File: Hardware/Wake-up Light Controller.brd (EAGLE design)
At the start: 85.7 x 54 mm, 47 parts, among them IC1 ST1S10, IC2 HT7333, IC3 DS3231/SO, IC4 ATMEGA328P_TQFP, J1 AVR-ISP, J2 Debug, J3 CR1632_3V, Q1 BSS138, Q2 BSS138, Q3 FDN306P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

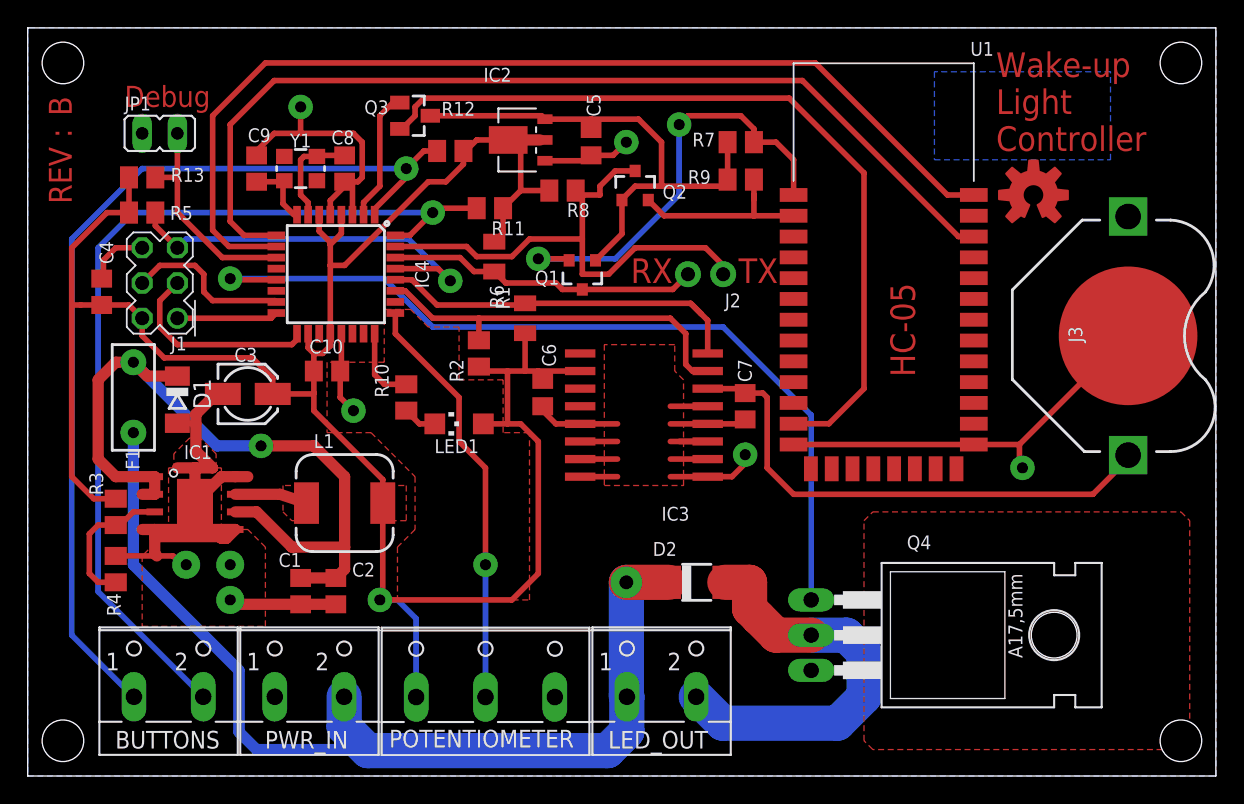
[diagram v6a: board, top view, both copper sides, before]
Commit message: Change text size
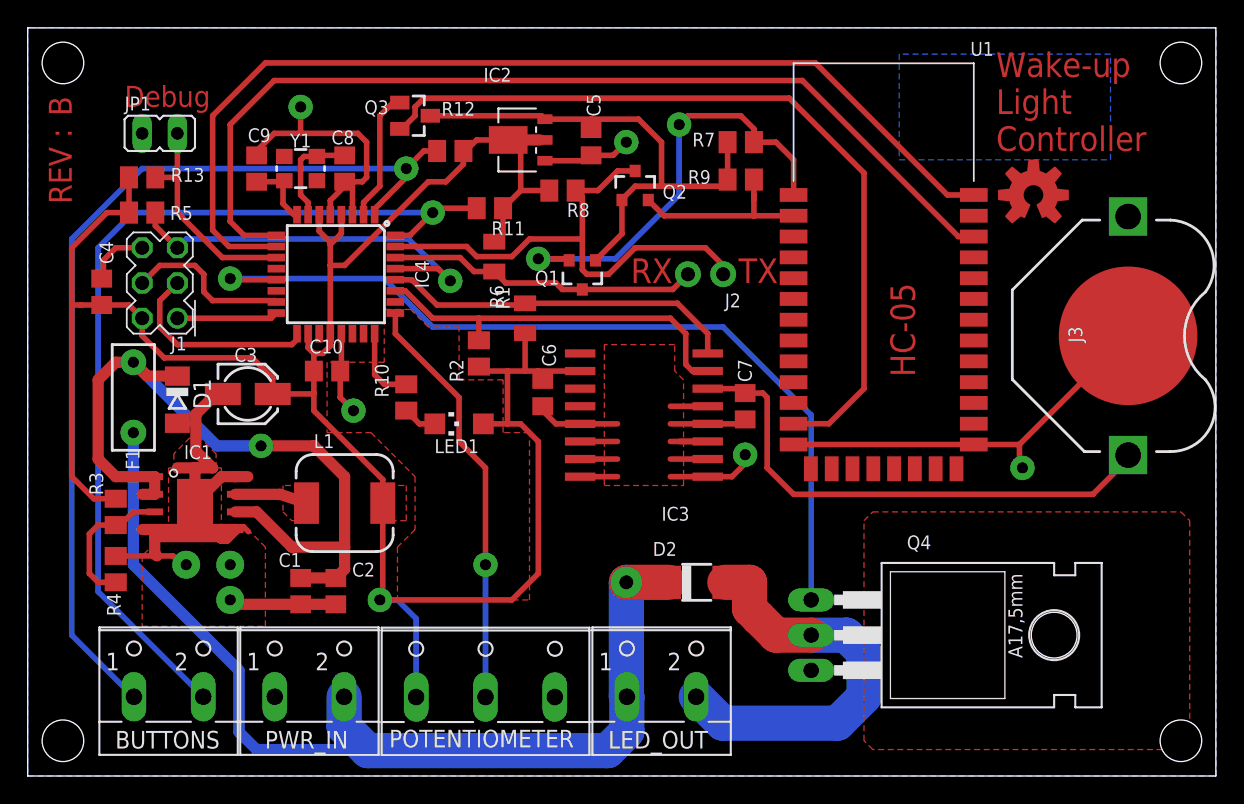
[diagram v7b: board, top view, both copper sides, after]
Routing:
- net GND: track 147.6 -> 149.4 mm
- net SCL: track 27.2 -> 25.7 mm
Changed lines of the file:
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@@
 <layer number="37" name="tTest" color="7" fill="1" visible="no" active="yes"/>
 <layer number="38" name="bTest" color="7" fill="1" visible="no" active="yes"/>
-<layer number="39" name="tKeepout" color="4" fill="11" visible="yes" active="yes"/>
-<layer number="40" name="bKeepout" color="1" fill="11" visible="yes" active="yes"/>
+<layer number="39" name="tKeepout" color="4" fill="11" visible="no" active="yes"/>
+<layer number="40" name="bKeepout" color="1" fill="11" visible="no" active="yes"/>
 <layer number="41" name="tRestrict" color="4" fill="10" visible="yes" active="yes"/>
 <layer number="42" name="bRestrict" color="1" fill="10" visible="yes" active="yes"/>
@@
 Light
 Controller</text>
-<text x="77.47" y="45.085" size="2.032" layer="42" font="vector" ratio="18" rot="SMR0">Heol Fief
+<text x="77.47" y="45.085" size="2.54" layer="42" font="vector" ratio="18" rot="SMR0">Heol Fief
 2017</text>
 <text x="62.23" y="35.56" size="1.778" layer="1" font="vector" ratio="18" rot="R270">HC-05</text>
@@
 <wire x1="23.495" y1="40.4176" x2="23.425" y2="40.4876" width="0.4064" layer="1"/>
 <polygon width="0.0254" layer="16" orphans="yes">
-<vertex x="65.405" y="50.8"/>
-<vertex x="65.405" y="44.45"/>
+<vertex x="62.865" y="52.07"/>
+<vertex x="62.865" y="44.45"/>
 <vertex x="78.105" y="44.45"/>
-<vertex x="78.105" y="50.8"/>
+<vertex x="78.105" y="52.07"/>
 </polygon>
 <wire x1="9.161" y1="17.78" x2="8.255" y2="17.78" width="0.8128" layer="1"/>
@@
 <wire x1="16.51" y1="45.085" x2="17.78" y2="46.355" width="0.4064" layer="1"/>
 <wire x1="23.330571875" y1="42.865" x2="22.86" y2="42.865" width="0.4064" layer="1"/>
-<wire x1="23.330571875" y1="42.865" x2="23.815" y2="42.865" width="0.4064" layer="1"/>
-<wire x1="23.815" y1="42.865" x2="24.13" y2="43.18" width="0.4064" layer="1"/>
+<wire x1="23.330571875" y1="42.865" x2="24.1325" y2="42.865" width="0.4064" layer="1"/>
+<wire x1="24.1325" y1="42.865" x2="24.4475" y2="43.18" width="0.4064" layer="1"/>
 <wire x1="23.425" y1="40.4876" x2="23.425" y2="42.770571875" width="0.4064" layer="1"/>
 <wire x1="23.425" y1="42.770571875" x2="23.330571875" y2="42.865" width="0.4064" layer="1"/>
@@
 <wire x1="12.065" y1="22.225" x2="10.795" y2="22.225" width="0.8128" layer="1"/>
 <wire x1="12.065" y1="22.225" x2="12.065" y2="19.685" width="0.8128" layer="1"/>
-<wire x1="14.969" y1="17.78" x2="14.334" y2="17.145" width="0.8128" layer="1"/>
+<wire x1="14.334" y1="17.145" x2="14.969" y2="17.78" width="0.8128" layer="1"/>
 <wire x1="14.334" y1="17.145" x2="13.97" y2="17.145" width="0.8128" layer="1"/>
 <wire x1="13.97" y1="17.145" x2="13.848325" y2="17.266675" width="0.8128" layer="1"/>
@@
 <contactref element="J3" pad="GND"/>
 <wire x1="55.245" y1="23.91" x2="68.245" y2="23.91" width="0.4064" layer="1"/>
-<wire x1="24.13" y1="45.72" x2="23.495" y2="46.355" width="0.4064" layer="1"/>
-<wire x1="19.685" y1="46.355" x2="23.495" y2="46.355" width="0.4064" layer="1"/>
+<wire x1="24.4475" y1="45.72" x2="23.8125" y2="46.355" width="0.4064" layer="1"/>
+<wire x1="19.685" y1="46.355" x2="23.8125" y2="46.355" width="0.4064" layer="1"/>
 <wire x1="19.685" y1="46.355" x2="17.78" y2="46.355" width="0.4064" layer="1"/>
-<wire x1="24.13" y1="43.18" x2="24.13" y2="45.72" width="0.4064" layer="1"/>
+<wire x1="24.4475" y1="43.18" x2="24.4475" y2="45.72" width="0.4064" layer="1"/>
 <via x="19.685" y="48.26" extent="1-16" drill="0.8" diameter="1.778"/>
 <wire x1="6.35" y1="38.1" x2="5.461" y2="37.211" width="0.4064" layer="1"/>
@@
 <wire x1="79.375" y1="31.75" x2="71.535" y2="23.91" width="0.4064" layer="1"/>
 <wire x1="19.685" y1="48.26" x2="19.685" y2="46.355" width="0.4064" layer="1"/>
+<wire x1="15.9258" y1="17.62125" x2="15.56511875" y2="17.981928125" width="0.4064" layer="1"/>
+<wire x1="15.56511875" y1="17.981928125" x2="14.94916875" y2="17.981928125" width="0.4064" layer="1"/>
 </signal>
 <signal name="+12V">
@@
 <wire x1="26.5176" y1="35.795" x2="27.705" y2="35.795" width="0.4064" layer="1"/>
 <wire x1="27.705" y1="35.795" x2="29.5275" y2="33.9725" width="0.4064" layer="1"/>
-<wire x1="49.05" y1="30.48" x2="49.05" y2="32.865" width="0.4064" layer="1"/>
-<wire x1="48.5775" y1="33.3375" x2="49.05" y2="32.865" width="0.4064" layer="1"/>
-<wire x1="48.5775" y1="33.3375" x2="47.879" y2="34.036" width="0.4064" layer="1"/>
+<wire x1="35.8775" y1="34.097" x2="46.8655" y2="34.097" width="0.4064" layer="1"/>
+<wire x1="46.8655" y1="34.097" x2="49.05" y2="31.9125" width="0.4064" layer="1"/>
+<wire x1="49.05" y1="31.9125" x2="49.05" y2="30.48" width="0.4064" layer="1"/>
 <wire x1="29.5275" y1="33.9725" x2="35.753" y2="33.9725" width="0.4064" layer="1"/>
 <wire x1="35.753" y1="33.9725" x2="35.8775" y2="34.097" width="0.4064" layer="1"/>
-<wire x1="35.8775" y1="34.097" x2="47.818" y2="34.097" width="0.4064" layer="1"/>
-<wire x1="47.818" y1="34.097" x2="48.5775" y2="33.3375" width="0.4064" layer="1"/>
 </signal>
 <signal name="SDA">
@@
 <contactref element="Q2" pad="3"/>
 <contactref element="R8" pad="2"/>
-<wire x1="42.375" y1="43.645" x2="43.815" y2="43.645" width="0.4064" layer="1"/>
+<wire x1="42.545" y1="43.645" x2="43.815" y2="43.645" width="0.4064" layer="1"/>
 <wire x1="48.895" y1="38.1" x2="43.815" y2="38.1" width="0.4064" layer="1"/>
 <wire x1="43.815" y1="38.1" x2="41.91" y2="36.195" width="0.4064" layer="1"/>
-<wire x1="41.91" y1="36.195" x2="40.005" y2="36.195" width="0.4064" layer="1"/>
+<wire x1="40.005" y1="38.735" x2="40.005" y2="36.5125" width="0.4064" layer="1"/>
+<wire x1="40.005" y1="36.5125" x2="40.3225" y2="36.195" width="0.4064" layer="1"/>
+<wire x1="40.3225" y1="36.195" x2="41.91" y2="36.195" width="0.4064" layer="1"/>
 <wire x1="50.165" y1="36.83" x2="48.895" y2="38.1" width="0.4064" layer="1"/>
 <contactref element="J2" pad="1"/>
 <wire x1="50.165" y1="36.195" x2="50.165" y2="36.83" width="0.4064" layer="1"/>
-<wire x1="41.275" y1="41.91" x2="41.275" y2="42.545" width="0.4064" layer="1"/>
-<wire x1="41.275" y1="42.545" x2="42.375" y2="43.645" width="0.4064" layer="1"/>
-<wire x1="39.52625" y1="42.2275" x2="39.84375" y2="41.91" width="0.4064" layer="1"/>
-<wire x1="39.84375" y1="41.91" x2="41.275" y2="41.91" width="0.4064" layer="1"/>
+<wire x1="40.005" y1="41.74875" x2="39.52625" y2="42.2275" width="0.4064" layer="1"/>
 <wire x1="26.5176" y1="38.195" x2="31.655" y2="38.195" width="0.4064" layer="1"/>
 <wire x1="31.655" y1="38.195" x2="32.385" y2="37.465" width="0.4064" layer="1"/>
 <wire x1="32.385" y1="37.465" x2="34.925" y2="37.465" width="0.4064" layer="1"/>
 <wire x1="34.925" y1="37.465" x2="36.195" y2="38.735" width="0.4064" layer="1"/>
-<wire x1="40.005" y1="38.735" x2="40.005" y2="36.195" width="0.4064" layer="1"/>
 <wire x1="40.005" y1="38.735" x2="40.005" y2="41.74875" width="0.4064" layer="1"/>
-<wire x1="40.005" y1="41.74875" x2="39.84375" y2="41.91" width="0.4064" layer="1"/>
 <wire x1="36.195" y1="38.735" x2="40.005" y2="38.735" width="0.4064" layer="1"/>
+<wire x1="39.52625" y1="42.2275" x2="41.1275" y2="42.2275" width="0.4064" layer="1"/>
+<wire x1="41.1275" y1="42.2275" x2="42.545" y2="43.645" width="0.4064" layer="1"/>
 </signal>
 <signal name="PAIRING">

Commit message: Add filtering cap, tweak layout
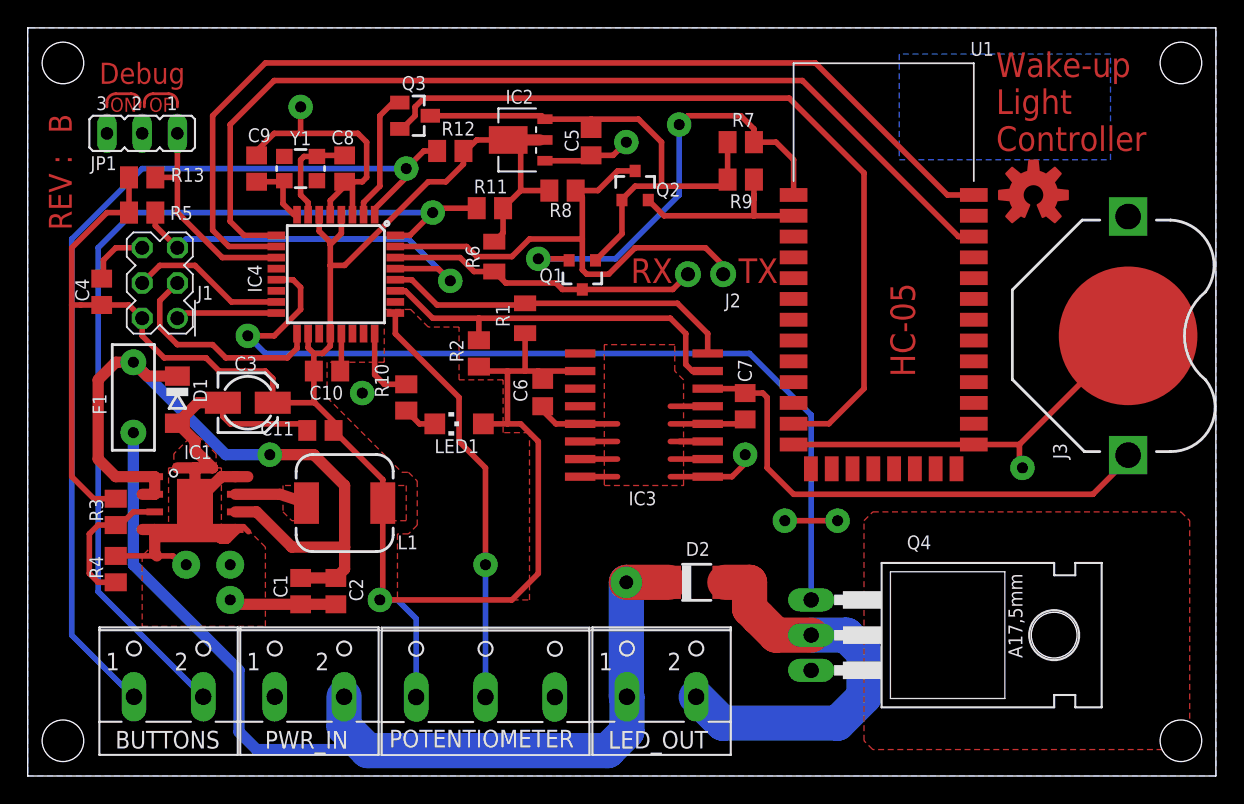
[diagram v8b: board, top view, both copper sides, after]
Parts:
- added C11: 4.7u, rcl:C0805
- F1: value 30V/0.5A -> PTC 0.5A
- JP1: value debug -> (none); device jumper:JP1 -> jumper:JP2
- moved JP1 1.27 mm to (8.26, 46.4), turned to 180 degrees
- moved C3 0.64 mm to (15.9, 26.9)
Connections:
- net +5V: now also C11.1
- net DEBUG: now also JP1.1; no longer JP1.2
- net GND: now also C11.2, JP1.2; no longer JP1.1
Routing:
- net GND: track 149.4 -> 157.2 mm, vias 8 -> 10
- net N$13: track 0.00 -> 3.54 mm
- net N$12: track 0.00 -> 3.54 mm
- net N$10: track 62.7 -> 64.5 mm
- net SCK: track 14.7 -> 15.9 mm
- net +5V: track 164.8 -> 165.6 mm
- net MOSI: track 12.0 -> 11.3 mm
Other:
- board text added: "OF"
- board text added: "ON"
